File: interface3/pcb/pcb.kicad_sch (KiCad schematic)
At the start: 54 parts, among them J1 PORT1, J2 PORT2, J3 PORT3/4, J4 POWER, SW1 Pico Run, T1 78602/8JC, T2 78602/8JC, U1 DS34LV86T, U2 DS34LV87T, U3 Pico_W

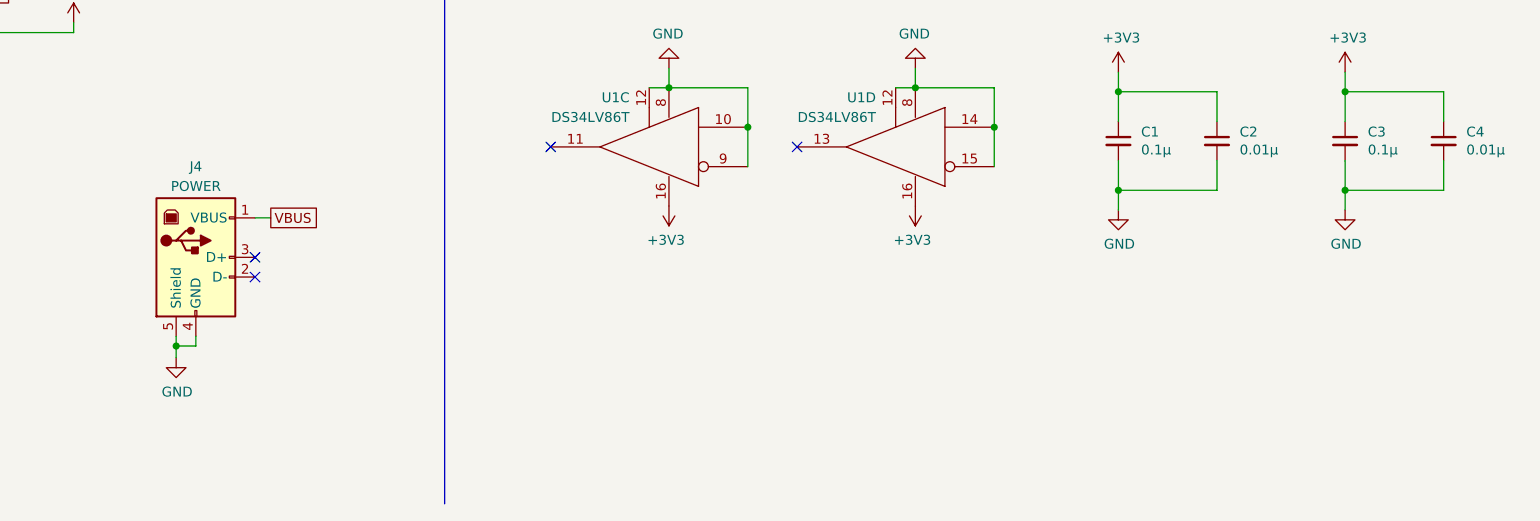
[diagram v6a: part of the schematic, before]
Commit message: fix PCB issues found in v1
closes #1, #2, #3
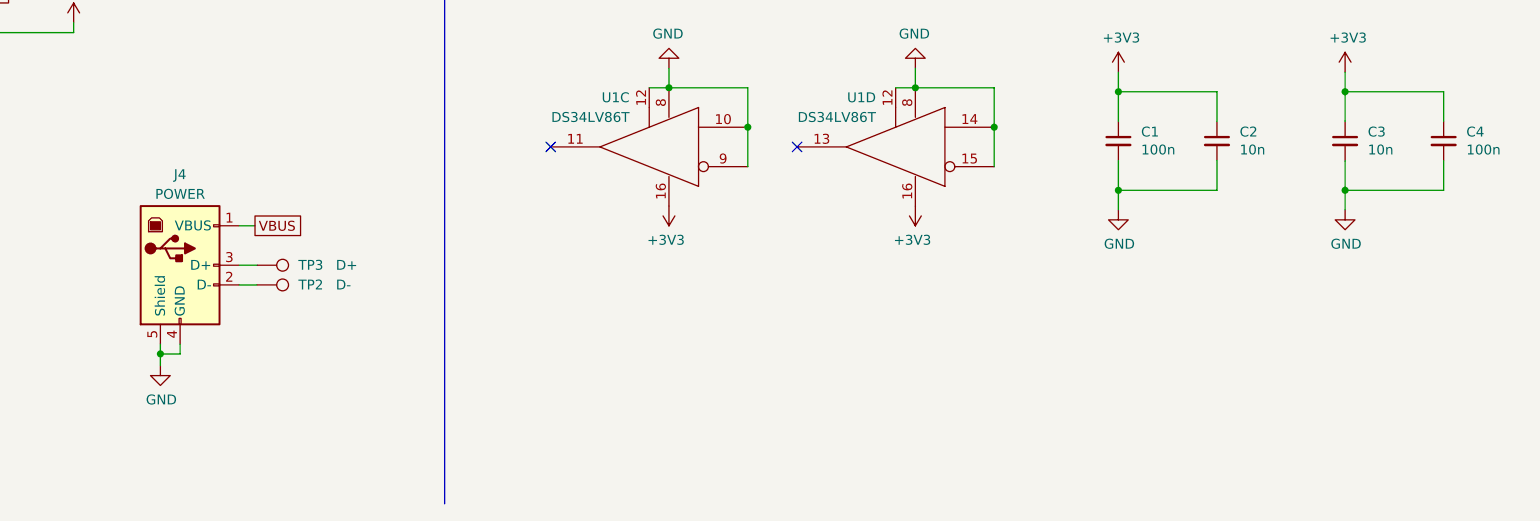
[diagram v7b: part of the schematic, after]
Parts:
- added TP2: D-, TestPoint:TestPoint_Pad_D2.0mm, symbol Connector:TestPoint
- added TP3: D+, TestPoint:TestPoint_Pad_D2.0mm, symbol Connector:TestPoint
- C1: value 0.1µ -> 100n
- C2: value 0.01µ -> 10n
- C3: value 0.1µ -> 10n
- C4: value 0.01µ -> 100n
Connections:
- net at J4.2 (D-): now also TP2.1
- net at J4.3 (D+): now also TP3.1
- no-connect marks 8 -> 6
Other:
- moved on the sheet: J4
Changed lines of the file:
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@@
   (junction (at 113.03 228.092) (diameter 0) (color 0 0 0 0)
   )
-  (junction (at 231.902 260.604) (diameter 0) (color 0 0 0 0)
+  (junction (at 229.87 261.62) (diameter 0) (color 0 0 0 0)
   )
   (junction (at 60.96 228.092) (diameter 0) (color 0 0 0 0)
@@
   (no_connect (at 161.036 74.93))
   (no_connect (at 161.036 90.17))
-  (no_connect (at 242.062 249.174))
   (no_connect (at 311.912 234.95))
   (no_connect (at 280.162 234.95))
   (no_connect (at 161.036 85.09))
-  (no_connect (at 242.062 251.714))
   (no_connect (at 161.036 80.01))
   (wire (pts (xy 124.206 72.39) (xy 125.476 72.39))
@@
     (stroke (width 0) (type default))
   )
+  (wire (pts (xy 240.03 252.73) (xy 242.316 252.73))
+    (stroke (width 0) (type default))
+  )
   (wire (pts (xy 353.314 225.298) (xy 353.314 227.838))
     (stroke (width 0) (type default))
@@
     (stroke (width 0) (type default))
   )
-  (wire (pts (xy 231.902 259.334) (xy 231.902 260.604))
+  (wire (pts (xy 229.87 260.35) (xy 229.87 261.62))
     (stroke (width 0) (type default))
   )
@@
     (stroke (width 0) (type default))
   )
+  (wire (pts (xy 240.03 250.19) (xy 242.316 250.19))
+    (stroke (width 0) (type default))
+  )
   (wire (pts (xy 187.198 217.678) (xy 184.404 217.678))
     (stroke (width 0) (type default))
@@
     (stroke (width 0) (type default))
   )
-  (wire (pts (xy 242.062 244.094) (xy 244.094 244.094))
+  (wire (pts (xy 240.03 245.11) (xy 242.062 245.11))
     (stroke (width 0) (type default))
   )
@@
     (stroke (width 0) (type default))
   )
-  (wire (pts (xy 231.902 260.604) (xy 231.902 262.128))
+  (wire (pts (xy 229.87 261.62) (xy 229.87 263.144))
     (stroke (width 0) (type default))
   )
@@
     (stroke (width 0) (type default))
   )
-  (wire (pts (xy 234.442 259.334) (xy 234.442 260.604))
+  (wire (pts (xy 232.41 260.35) (xy 232.41 261.62))
     (stroke (width 0) (type default))
   )
@@
     (stroke (width 0) (type default))
   )
-  (wire (pts (xy 234.442 260.604) (xy 231.902 260.604))
+  (wire (pts (xy 232.41 261.62) (xy 229.87 261.62))
     (stroke (width 0) (type default))
   )
@@
     )
   )
-  (global_label "VBUS" (shape passive) (at 244.094 244.094 0)
+  (global_label "VBUS" (shape passive) (at 242.062 245.11 0)
     (effects (font (size 1.27 1.27)) (justify left))
-    (property "Intersheetrefs" "${INTERSHEET_REFS}" (at 244.094 244.094 0)
+    (property "Intersheetrefs" "${INTERSHEET_REFS}" (at 242.062 245.11 0)
       (effects (font (size 1.27 1.27)) hide)
     )
@@
     )
   )
-  (symbol (lib_id "power:GND") (at 231.902 262.128 0) (unit 1)
+  (symbol (lib_id "power:GND") (at 229.87 263.144 0) (unit 1)
     (in_bom yes) (on_board yes) (dnp no)
-    (property "Reference" "#PWR038" (at 231.902 268.478 0)
+    (property "Reference" "#PWR038" (at 229.87 269.494 0)
       (effects (font (size 1.27 1.27)) hide)
     )
-    (property "Value" "GND" (at 232.029 266.5222 0)
+    (property "Value" "GND" (at 229.997 267.5382 0)
       (effects (font (size 1.27 1.27)))
     )
-    (property "Footprint" "" (at 231.902 262.128 0)
+    (property "Footprint" "" (at 229.87 263.144 0)
       (effects (font (size 1.27 1.27)) hide)
     )
-    (property "Datasheet" "" (at 231.902 262.128 0)
+    (property "Datasheet" "" (at 229.87 263.144 0)
       (effects (font (size 1.27 1.27)) hide)
     )
@@
     )
   )
-  (symbol (lib_id "Connector:USB_B") (at 234.442 249.174 0) (unit 1)
+  (symbol (lib_id "Connector:USB_B") (at 232.41 250.19 0) (unit 1)
     (in_bom yes) (on_board yes) (dnp no) (fields_autoplaced)
-    (property "Reference" "J4" (at 234.442 237.49 0)
+    (property "Reference" "J4" (at 232.41 238.506 0)
       (effects (font (size 1.27 1.27)))
     )
-    (property "Value" "POWER" (at 234.442 240.03 0)
+    (property "Value" "POWER" (at 232.41 241.046 0)
       (effects (font (size 1.27 1.27)))
     )
-    (property "Footprint" "Connector_USB:USB_B_OST_USB-B1HSxx_Horizontal" (at 238.252 250.444 0)
+    (property "Footprint" "Connector_USB:USB_B_OST_USB-B1HSxx_Horizontal" (at 236.22 251.46 0)
       (effects (font (size 1.27 1.27)) hide)
     )
-    (property "Datasheet" " ~" (at 238.252 250.444 0)
+    (property "Datasheet" " ~" (at 236.22 251.46 0)
       (effects (font (size 1.27 1.27)) hide)
     )
@@
     )
   )
+  (symbol (lib_id "Connector:TestPoint") (at 242.316 252.73 270) (unit 1)
+    (in_bom yes) (on_board yes) (dnp no)
+    (property "Reference" "TP2" (at 247.65 252.73 90)
+      (effects (font (size 1.27 1.27)) (justify left))
+    )
+    (property "Value" "D-" (at 252.476 252.73 90)
+      (effects (font (size 1.27 1.27)) (justify left))
+    )
+    (property "Footprint" "TestPoint:TestPoint_Pad_D2.0mm" (at 242.316 257.81 0)
+      (effects (font (size 1.27 1.27)) hide)
+    )
+    (property "Datasheet" "~" (at 242.316 257.81 0)
+      (effects (font (size 1.27 1.27)) hide)
+    )
+    (pin "1")
+    (instances
+      (project "pcb"
+        (path "/526cd2dc-8794-4bb6-97c2-9b545ee4fe34"
+          (reference "TP2") (unit 1)
+        )
+      )
+    )
+  )
   (symbol (lib_id "Interface_LineDriver:MC3486N") (at 301.752 137.922 180) (unit 1)
     (in_bom yes) (on_board yes) (dnp no)
@@
       (effects (font (size 1.27 1.27)) (justify left))
     )
-    (property "Value" "0.1µ" (at 356.235 235.331 0)
+    (property "Value" "100n" (at 356.235 235.331 0)
       (effects (font (size 1.27 1.27)) (justify left))
     )
@@
     )
   )
+  (symbol (lib_id "Connector:TestPoint") (at 242.316 250.19 270) (unit 1)
+    (in_bom yes) (on_board yes) (dnp no)
+    (property "Reference" "TP3" (at 247.65 250.19 90)
+      (effects (font (size 1.27 1.27)) (justify left))
+    )
+    (property "Value" "D+" (at 252.476 250.19 90)
+      (effects (font (size 1.27 1.27)) (justify left))
+    )
+    (property "Footprint" "TestPoint:TestPoint_Pad_D2.0mm" (at 242.316 255.27 0)
+      (effects (font (size 1.27 1.27)) hide)
+    )
+    (property "Datasheet" "~" (at 242.316 255.27 0)
+      (effects (font (size 1.27 1.27)) hide)
+    )
+    (pin "1")
+    (instances
+      (project "pcb"
+        (path "/526cd2dc-8794-4bb6-97c2-9b545ee4fe34"
+          (reference "TP3") (unit 1)
+        )
+      )
+    )
+  )
   (symbol (lib_id "Device:R") (at 322.072 168.402 90) (mirror x) (unit 1)
     (in_bom yes) (on_board yes) (dnp no)
@@
       (effects (font (size 1.27 1.27)) (justify right))
     )
-    (property "Value" "0.01µ" (at 368.935 235.331 0)
+    (property "Value" "10n" (at 368.935 235.331 0)
       (effects (font (size 1.27 1.27)) (justify right))
     )
@@
       (effects (font (size 1.27 1.27)) (justify left))
     )
-    (property "Value" "0.1µ" (at 385.445 235.331 0)
+    (property "Value" "10n" (at 385.445 235.331 0)
       (effects (font (size 1.27 1.27)) (justify left))
     )
@@
       (effects (font (size 1.27 1.27)) (justify right))
     )
-    (property "Value" "0.01µ" (at 398.145 235.331 0)
+    (property "Value" "100n" (at 398.145 235.331 0)
       (effects (font (size 1.27 1.27)) (justify right))
     )
